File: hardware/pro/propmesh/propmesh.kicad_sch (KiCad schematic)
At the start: 0 parts

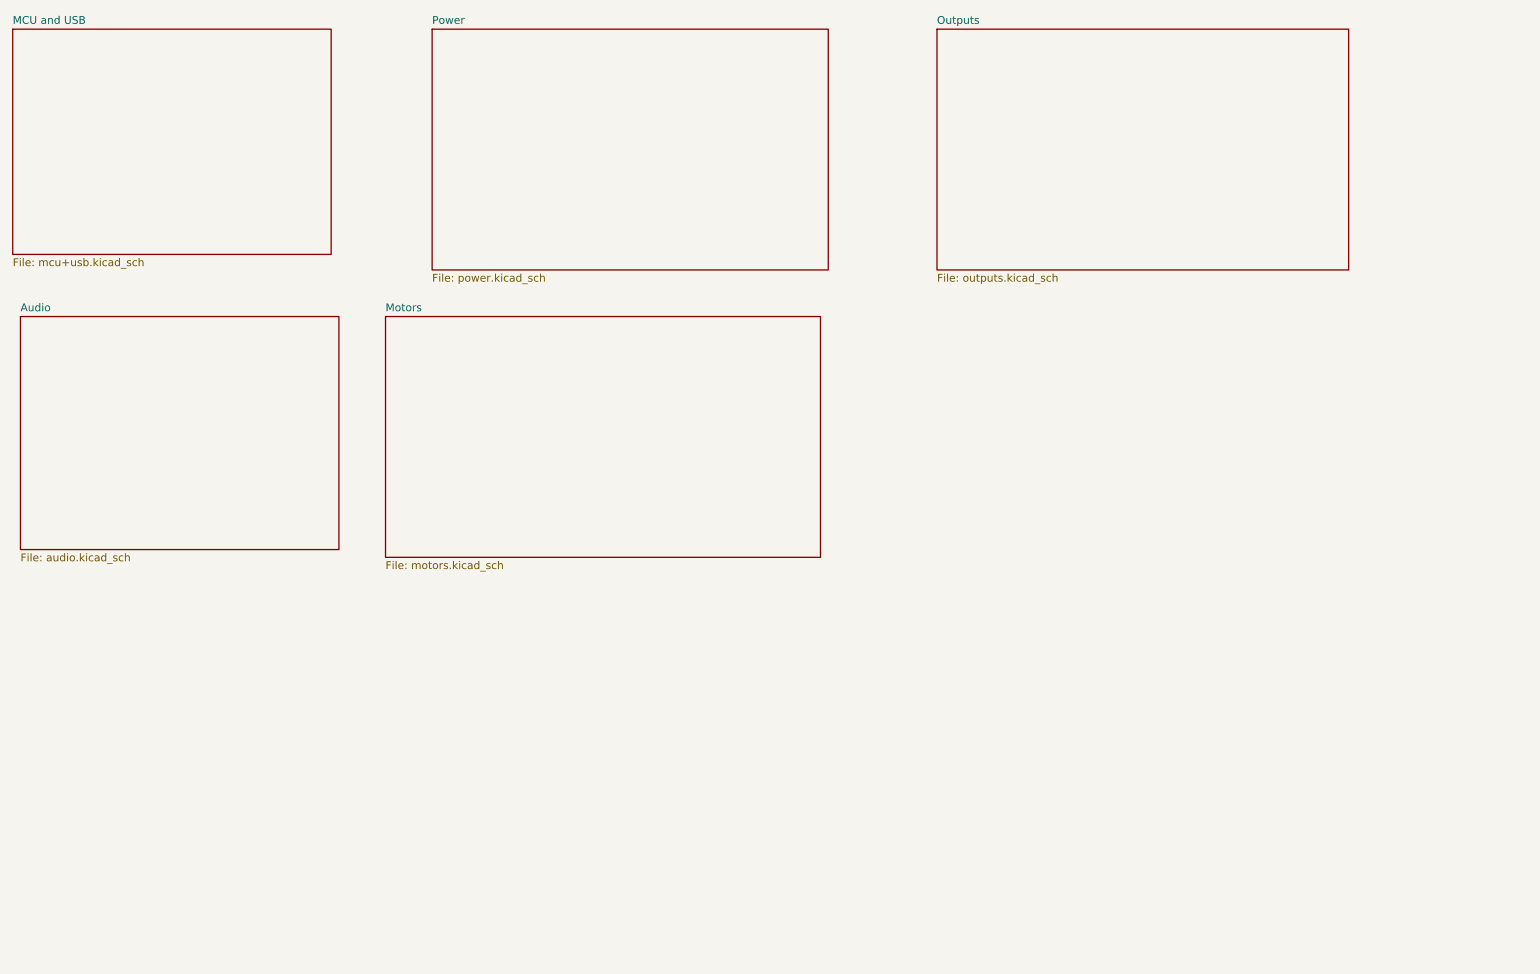
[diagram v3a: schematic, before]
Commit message: Sheet 07 (sensors + expansion) captured; sheet 05 spec ready
Sheet 07 drawn and verified: 3 clamped digital inputs (+ PIR header),
2 halved analog inputs, TSOP38238 on filtered 3V3, Qwiic (SH-1.0 clone
C7430446 — genuine JST stock-dead), 2x5 expansion header with GPIO45/46
strap protection. checknet all green, ERC clean bar the 4 LED labels
awaiting sheet 05. D2_MID global on motors + sensors sheets so
expansion pin 9 rides GPIO43's 1k.

Sheet 05 spec: AHCT125 moved to SOIC-14 C155176 (TSSOP dead at JLC),
strip 2 = 2x DG128-02P (04P dead), WS2812B-MINI-X2 status pixel
imported + datasheet-verified (pins, land pattern, VIH math).

Cost: all seven blocks now verified; parts subtotal $31.93,
duty-paid ~$48.55. Open item #2 mostly resolved (residual: JLC order
UI check before first PCBA run).

New repo rule after the C_A1 collision: spec refs are project-global —
never reuse one across sheet yamls (audio R_D3 -> R_DAT3, sensor caps
-> C_AN1/2).

Co-Authored-By: Claude Fable 5 <noreply@anthropic.com>
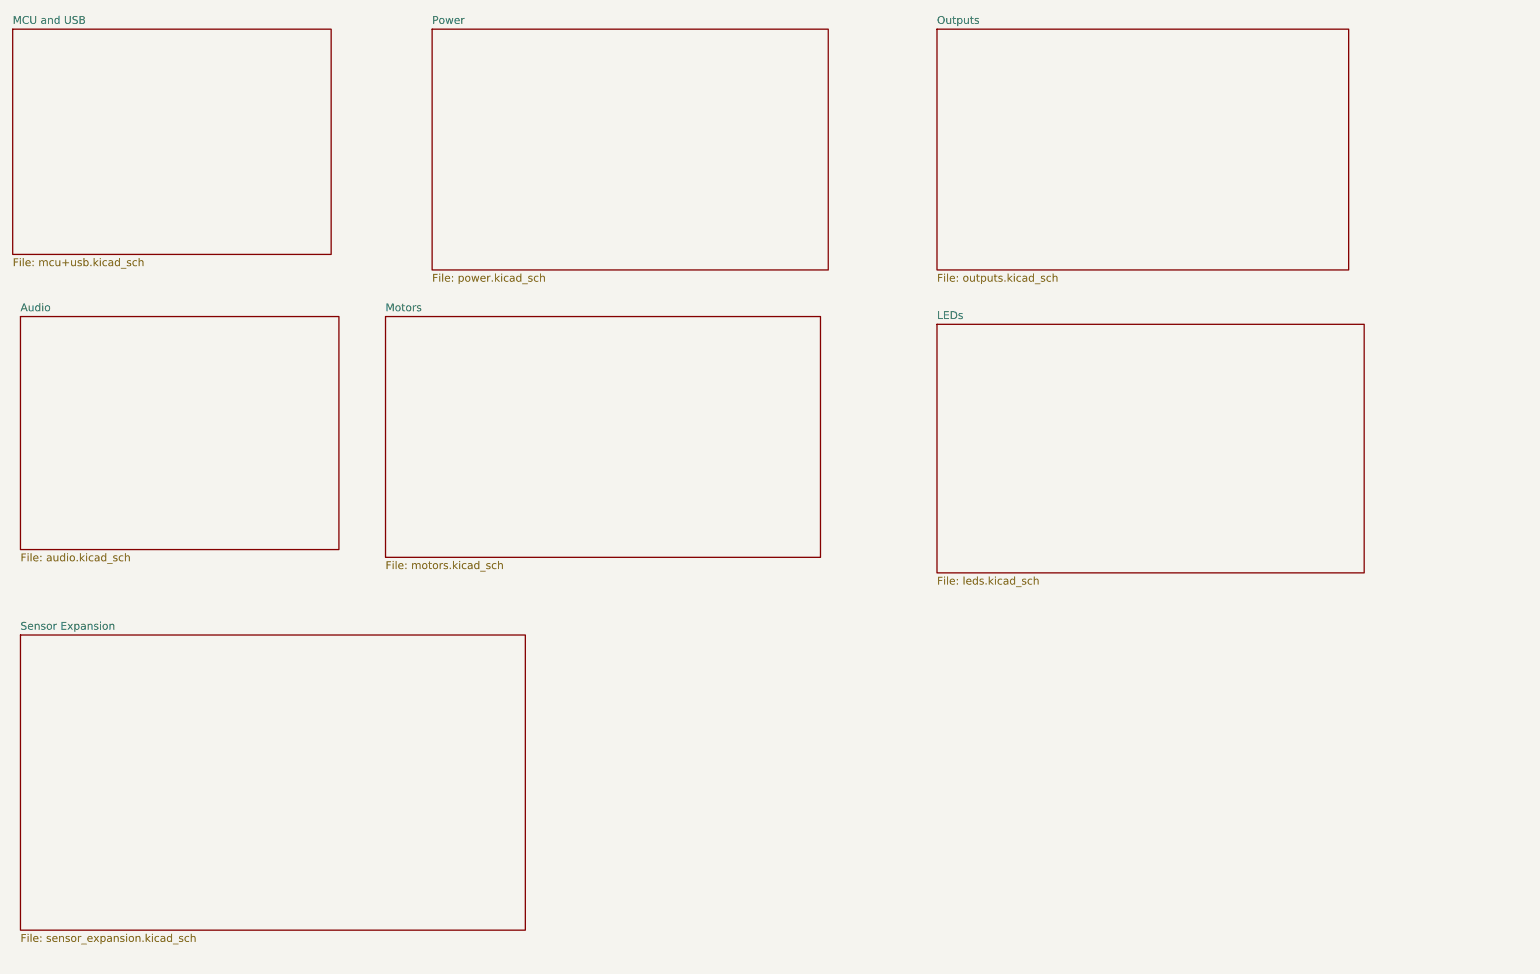
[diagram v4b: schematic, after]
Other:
- added sheet LEDs (leds.kicad_sch)
- added sheet Sensor Expansion (sensor_expansion.kicad_sch)
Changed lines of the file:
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@@
+		)
+	)
+	(sheet
+		(at 175.26 71.12)
+		(size 69.85 40.64)
+		(exclude_from_sim no)
+		(in_bom yes)
+		(on_board yes)
+		(dnp no)
+		(fields_autoplaced yes)
+		(stroke
+			(width 0.1524)
+			(type solid)
+		)
+		(fill
+			(color 0 0 0 0)
+		)
+		(property "Sheetname" "LEDs"
+			(at 175.26 70.4084 0)
+			(show_name no)
+			(do_not_autoplace no)
+			(effects
+				(font
+					(size 1.27 1.27)
+				)
+				(justify left bottom)
+			)
+		)
+		(property "Sheetfile" "leds.kicad_sch"
+			(at 175.26 112.3446 0)
+			(show_name no)
+			(do_not_autoplace no)
+			(effects
+				(font
+					(size 1.27 1.27)
+				)
+				(justify left top)
+			)
+		)
+		(instances
+			(project "propmesh"
+				(path "/6aa579d1-bfe0-499b-882d-72f52ff6d36c"
+					(page "7")
+				)
+			)
+		)
+	)
+	(sheet
+		(at 25.4 121.92)
+		(size 82.55 48.26)
+		(exclude_from_sim no)
+		(in_bom yes)
+		(on_board yes)
+		(dnp no)
+		(fields_autoplaced yes)
+		(stroke
+			(width 0.1524)
+			(type solid)
+		)
+		(fill
+			(color 0 0 0 0)
+		)
+		(property "Sheetname" "Sensor Expansion"
+			(at 25.4 121.2084 0)
+			(show_name no)
+			(do_not_autoplace no)
+			(effects
+				(font
+					(size 1.27 1.27)
+				)
+				(justify left bottom)
+			)
+		)
+		(property "Sheetfile" "sensor_expansion.kicad_sch"
+			(at 25.4 170.7646 0)
+			(show_name no)
+			(do_not_autoplace no)
+			(effects
+				(font
+					(size 1.27 1.27)
+				)
+				(justify left top)
+			)
+		)
+		(instances
+			(project "propmesh"
+				(path "/6aa579d1-bfe0-499b-882d-72f52ff6d36c"
+					(page "8")
+				)
+			)
 		)
 	)

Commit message: Sheet 08 (test points) + staged-power link headers; board synced 239/239
Sheet 08: 33 GPIO test points, 6 rail pads, DNP strap pad on GPIO 3 —
labels, values, wires and footprints generated from the yaml
(tools-side, not typed), power symbols cloned with every coordinate
shifted so texts travel with their parts. Sheet 01: JP_VIN / JP_5V /
JP_3V3 2-pin headers + shunts between input → 5 V buck → +5V rail →
+3V3 rail (spec §2.6 staged bring-up; a meter across a pulled shunt
reads that rail's current); PWR_FLAGs re-homed to the far side of each
jumper. Values use Colin's JP_* names; jumper pin numbering follows
the drawing.

All eight sheets green, ERC 0 violations, board updated with orphan
deletion: 239 footprints for 239 symbols, none differing.

checknet.py: extras from other sheets no longer crash the report or
the diagram renderer.

Co-Authored-By: Claude Fable 5.1 <noreply@anthropic.com>
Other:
- added sheet Test Points (testpoints.kicad_sch)
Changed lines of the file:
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@@
+	)
+	(sheet
+		(at 119.38 121.92)
+		(size 74.93 50.8)
+		(exclude_from_sim no)
+		(in_bom yes)
+		(on_board yes)
+		(dnp no)
+		(fields_autoplaced yes)
+		(stroke
+			(width 0.1524)
+			(type solid)
+		)
+		(fill
+			(color 0 0 0 0)
+		)
+		(property "Sheetname" "Test Points"
+			(at 119.38 121.2084 0)
+			(show_name no)
+			(do_not_autoplace no)
+			(effects
+				(font
+					(size 1.27 1.27)
+				)
+				(justify left bottom)
+			)
+		)
+		(property "Sheetfile" "testpoints.kicad_sch"
+			(at 119.38 173.3046 0)
+			(show_name no)
+			(do_not_autoplace no)
+			(effects
+				(font
+					(size 1.27 1.27)
+				)
+				(justify left top)
+			)
+		)
+		(instances
+			(project "propmesh"
+				(path "/6aa579d1-bfe0-499b-882d-72f52ff6d36c"
+					(page "9")
+				)
+			)
+		)
 	)
 	(sheet
